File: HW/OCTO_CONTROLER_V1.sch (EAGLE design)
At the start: 58 parts, among them IC1 CXDM4060P, IC2 AOZ1284PI, J1 DC_POWER, Q1 CXDM4060P, Q10 DTDG23YP, Q2 CXDM4060P, Q3 DTC114EUA, Q4 DTC114EUA, Q5 DTC114EUA, Q6 DTC114EUA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

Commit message: RENAME PCB DESIGN FILE
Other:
- note added: "OCTO PRINTER CONTROLER V1.0"
- note removed: "OCTO PRINTER POWER & LED CONTROLER V1.0"
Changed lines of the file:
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@@
 <sheet>
 <plain>
-<text x="-208.28" y="53.34" size="10.16" layer="97">OCTO PRINTER POWER &amp; LED CONTROLER V1.0</text>
+<text x="-208.28" y="53.34" size="10.16" layer="97">OCTO PRINTER  CONTROLER V1.0</text>
 <wire x1="-208.28" y1="-53.34" x2="-119.38" y2="-53.34" width="0.1524" layer="97"/>
 <wire x1="-208.28" y1="-144.78" x2="-119.38" y2="-144.78" width="0.1524" layer="97"/>

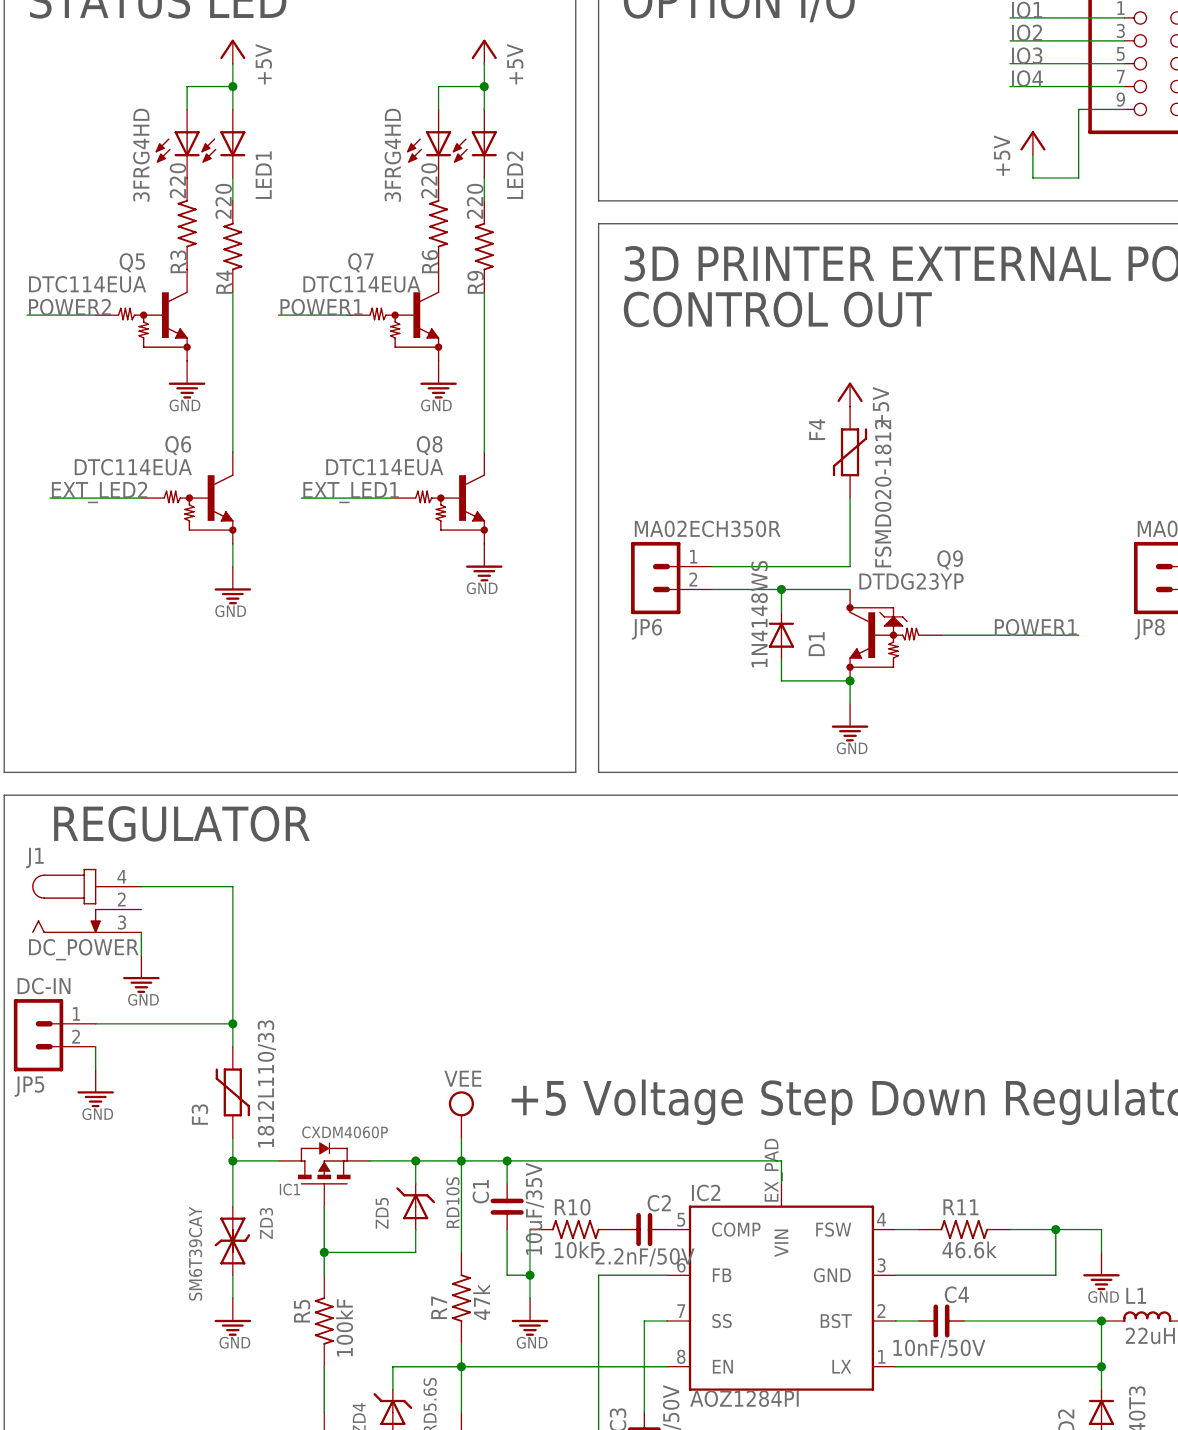
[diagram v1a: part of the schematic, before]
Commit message: LED 저항값 수정
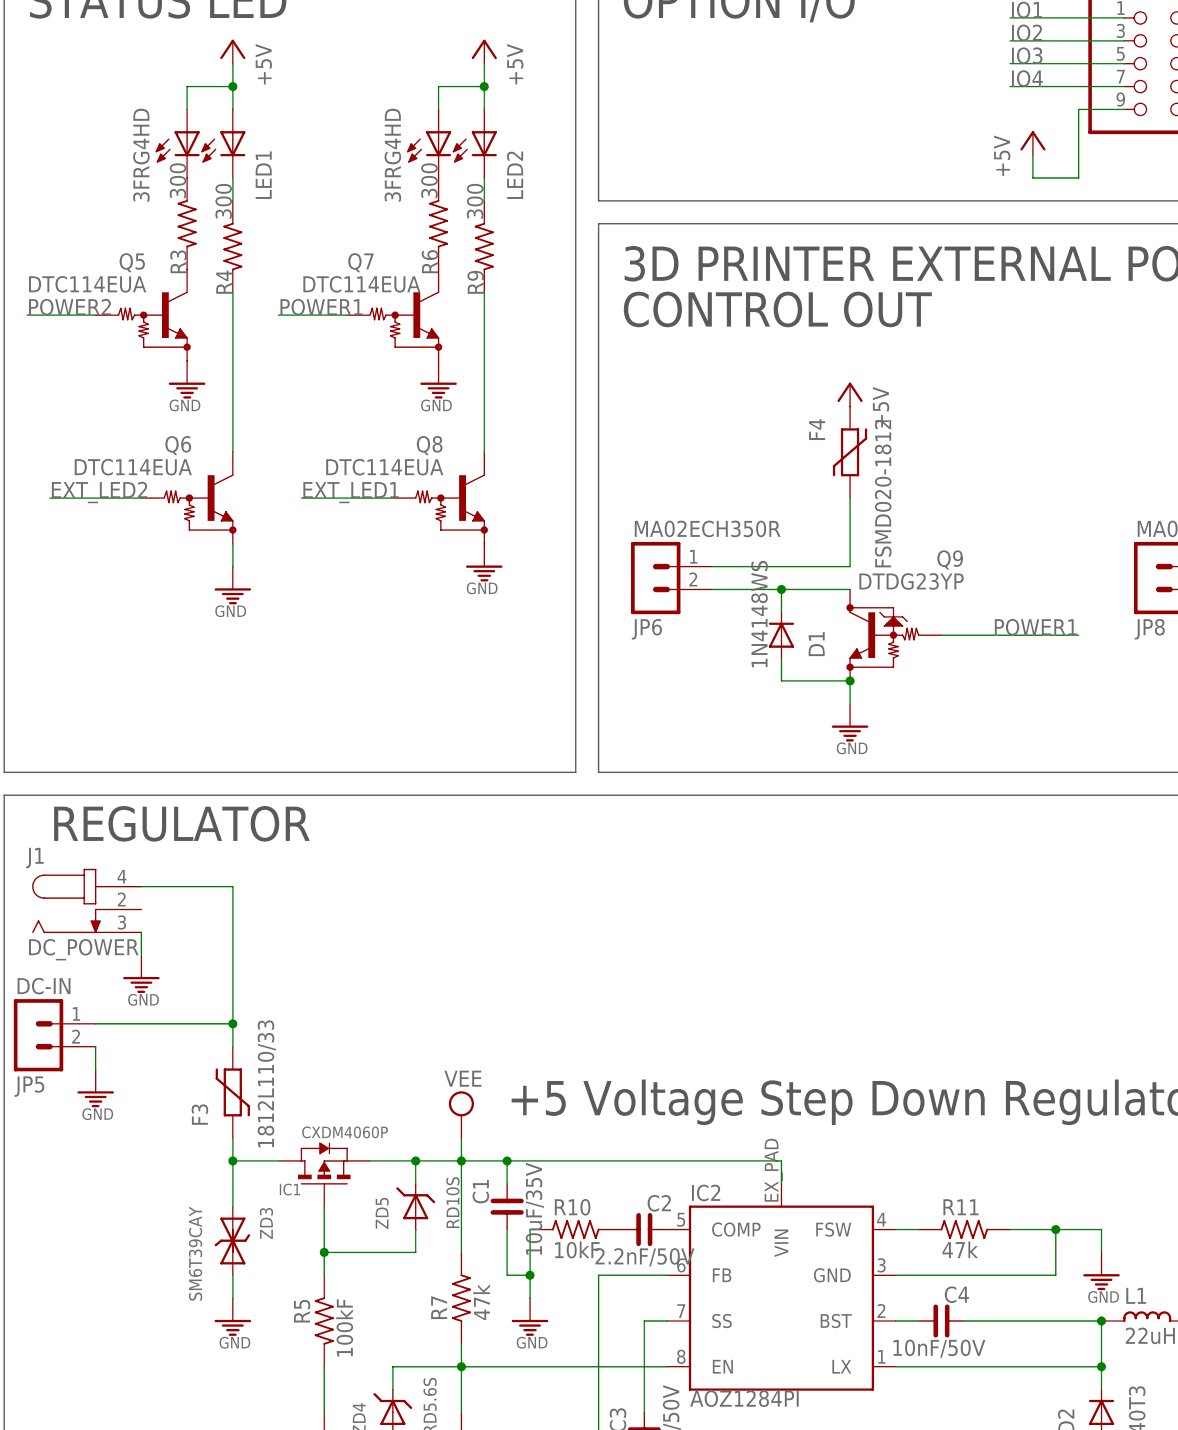
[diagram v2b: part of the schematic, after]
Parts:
- R11: value 46.6k -> 47k
- R3, R4, R6, R9: value 220 -> 300
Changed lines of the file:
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@@
 <part name="R10" library="cona_lib" deviceset="R_" device="0603" value="10kF"/>
 <part name="C2" library="cona_lib" deviceset="C_" device="0603" value="2.2nF/50V"/>
-<part name="R11" library="cona_lib" deviceset="R_" device="0603" value="46.6k"/>
+<part name="R11" library="cona_lib" deviceset="R_" device="0603" value="47k"/>
 <part name="C3" library="cona_lib" deviceset="C_" device="0603" value="0.1uF/50V"/>
 <part name="D2" library="diode" deviceset="DIODE-" device="SMC" value="MBRS540T3"/>
@@
 <part name="P+6" library="supply1" deviceset="+5V" device=""/>
 <part name="F4" library="ptc-littlefuse" deviceset="1812L" device="" value="FSMD020-1812"/>
-<part name="R6" library="cona_lib" deviceset="R_" device="0603" value="220"/>
-<part name="R9" library="cona_lib" deviceset="R_" device="0603" value="220"/>
+<part name="R6" library="cona_lib" deviceset="R_" device="0603" value="300"/>
+<part name="R9" library="cona_lib" deviceset="R_" device="0603" value="300"/>
 <part name="PE4" library="cona_lib" deviceset="GND" device=""/>
 <part name="PE20" library="cona_lib" deviceset="GND" device=""/>
@@
 <part name="Q7" library="cona_lib" deviceset="DTC114EUA" device=""/>
 <part name="Q8" library="cona_lib" deviceset="DTC114EUA" device=""/>
-<part name="R3" library="cona_lib" deviceset="R_" device="0603" value="220"/>
-<part name="R4" library="cona_lib" deviceset="R_" device="0603" value="220"/>
+<part name="R3" library="cona_lib" deviceset="R_" device="0603" value="300"/>
+<part name="R4" library="cona_lib" deviceset="R_" device="0603" value="300"/>
 <part name="PE7" library="cona_lib" deviceset="GND" device=""/>
 <part name="PE8" library="cona_lib" deviceset="GND" device=""/>
